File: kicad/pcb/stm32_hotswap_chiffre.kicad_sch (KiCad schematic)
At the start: 23 parts, among them J1 USB_C_Receptacle_USB2.0, J2 OLED I2C, U1 STM32F072CBT6, U2 PRTR5V0U2X

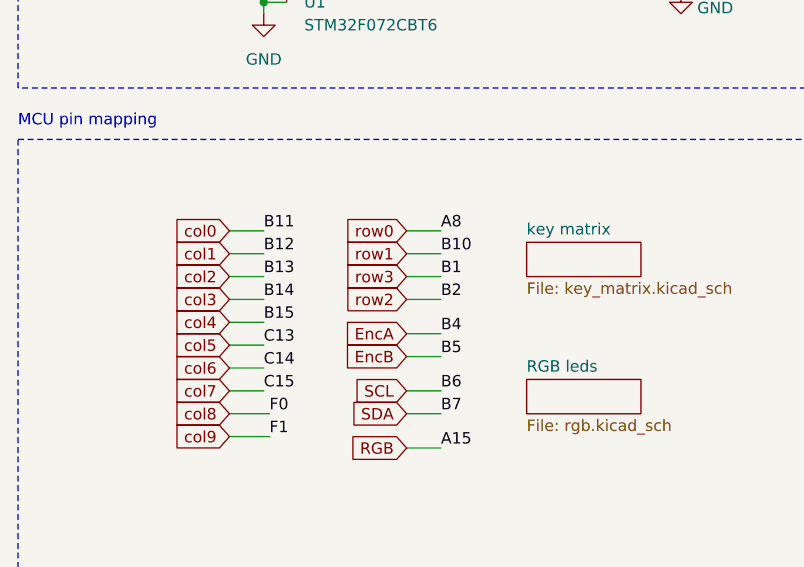
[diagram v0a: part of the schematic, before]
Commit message: fix pin order
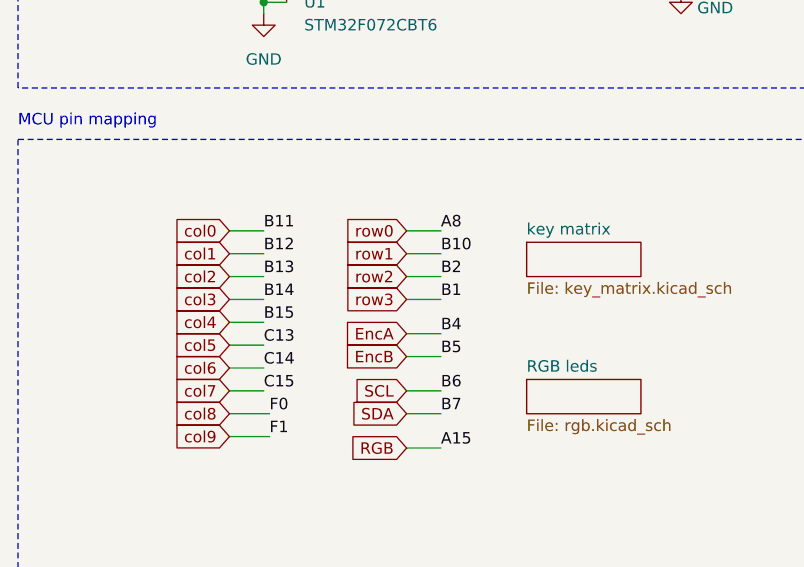
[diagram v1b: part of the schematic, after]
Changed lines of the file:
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@@
     (stroke (width 0) (type default))
   )
-  (wire (pts (xy 57.15 140.97) (xy 60.96 140.97))
+  (wire (pts (xy 57.15 143.51) (xy 60.96 143.51))
     (stroke (width 0) (type default))
   )
@@
     (stroke (width 0) (type default))
   )
-  (wire (pts (xy 57.15 143.51) (xy 60.96 143.51))
+  (wire (pts (xy 57.15 140.97) (xy 60.96 140.97))
     (stroke (width 0) (type default))
   )
@@
     (effects (font (size 1.27 1.27)) (justify left bottom))
   )
-  (label "B1" (at 60.96 140.97 0) (fields_autoplaced)
+  (label "B1" (at 60.96 143.51 0) (fields_autoplaced)
     (effects (font (size 1.27 1.27)) (justify left bottom))
   )
@@
     (effects (font (size 1.27 1.27)) (justify right bottom))
   )
-  (label "B2" (at 60.96 143.51 0) (fields_autoplaced)
+  (label "B2" (at 60.96 140.97 0) (fields_autoplaced)
     (effects (font (size 1.27 1.27)) (justify left bottom))
   )
@@
     )
   )
-  (global_label "row2" (shape input) (at 57.15 143.51 180) (fields_autoplaced)
-    (effects (font (size 1.27 1.27)) (justify right))
-    (property "Intersheetrefs" "${INTERSHEET_REFS}" (at 49.769 143.51 0)
+  (global_label "row2" (shape input) (at 57.15 140.97 180) (fields_autoplaced)
+    (effects (font (size 1.27 1.27)) (justify right))
+    (property "Intersheetrefs" "${INTERSHEET_REFS}" (at 49.769 140.97 0)
       (effects (font (size 1.27 1.27)) (justify right) hide)
     )
@@
     )
   )
-  (global_label "row3" (shape input) (at 57.15 140.97 180) (fields_autoplaced)
-    (effects (font (size 1.27 1.27)) (justify right))
-    (property "Intersheetrefs" "${INTERSHEET_REFS}" (at 49.769 140.97 0)
-      (effects (font (size 1.27 1.27)) (justify right) hide)
-    )
+  (global_label "row3" (shape input) (at 57.15 143.51 180) (fields_autoplaced)
+    (effects (font (size 1.27 1.27)) (justify right))
+    (property "Intersheetrefs" "${INTERSHEET_REFS}" (at 49.769 143.51 0)
+      (effects (font (size 1.27 1.27)) (justify right) hide)
+    )
